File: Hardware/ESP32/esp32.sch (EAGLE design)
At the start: 50 parts, among them J1 1x6, M1 BATTERY-CHARGER-LI-PROT, T1 BC847, U1 ESP-WROOM-32, U21 DC-DC-STEP-UP

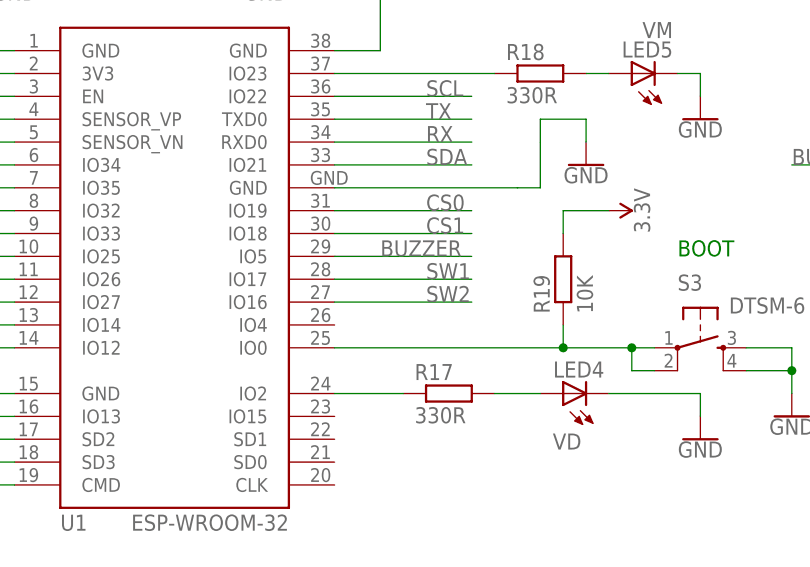
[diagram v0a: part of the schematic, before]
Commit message: Buzzer -> GPIO04
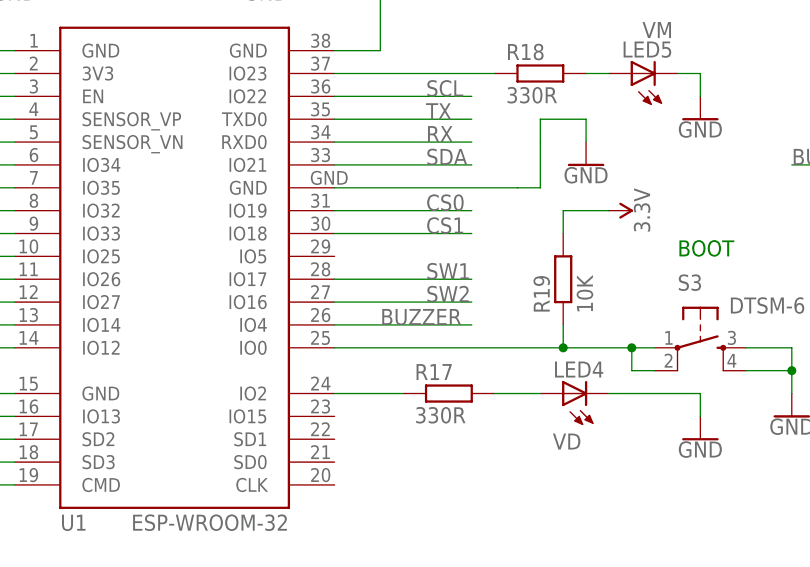
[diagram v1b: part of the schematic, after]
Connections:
- net BUZZER: now also U1.IO4; no longer U1.IO5
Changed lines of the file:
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@@
 <net name="BUZZER" class="0">
-<segment>
-<pinref part="U1" gate="G$1" pin="IO5"/>
-<wire x1="121.92" y1="129.54" x2="137.16" y2="129.54" width="0.1524" layer="91"/>
-<label x="127" y="129.54" size="1.778" layer="95"/>
-</segment>
 <segment>
 <pinref part="R20" gate="G$1" pin="1"/>
@@
 <label x="172.72" y="139.7" size="1.778" layer="95"/>
 </segment>
+<segment>
+<pinref part="U1" gate="G$1" pin="IO4"/>
+<wire x1="121.92" y1="121.92" x2="137.16" y2="121.92" width="0.1524" layer="91"/>
+<label x="127" y="121.92" size="1.778" layer="95"/>
+</segment>
 </net>
